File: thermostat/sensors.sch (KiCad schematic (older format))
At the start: 12 parts, among them U2 MCP7940N-xMS, U3 MCP9844, U4 AT24C512, Y3 32.768KHz 20PPM 3.2x1.5mm 7PF

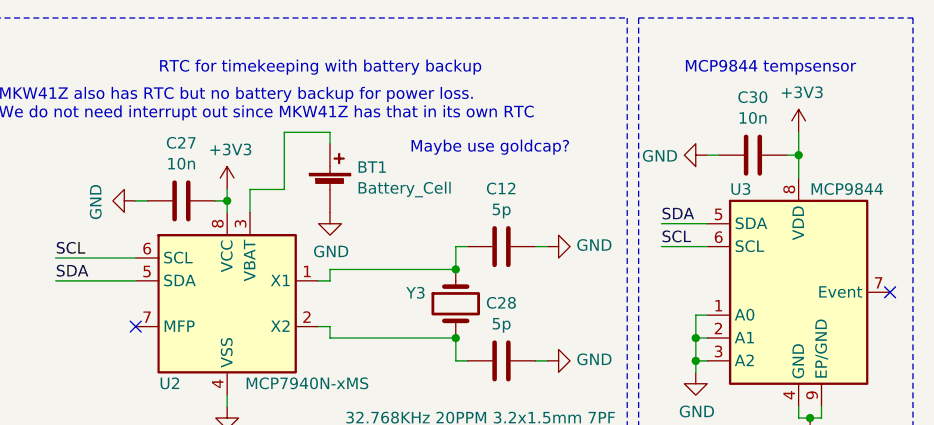
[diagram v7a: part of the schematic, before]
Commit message: Finished layouting tempsensor and thermostat. Parts are ordered from Mouser, PCB ordered from beta-layout.
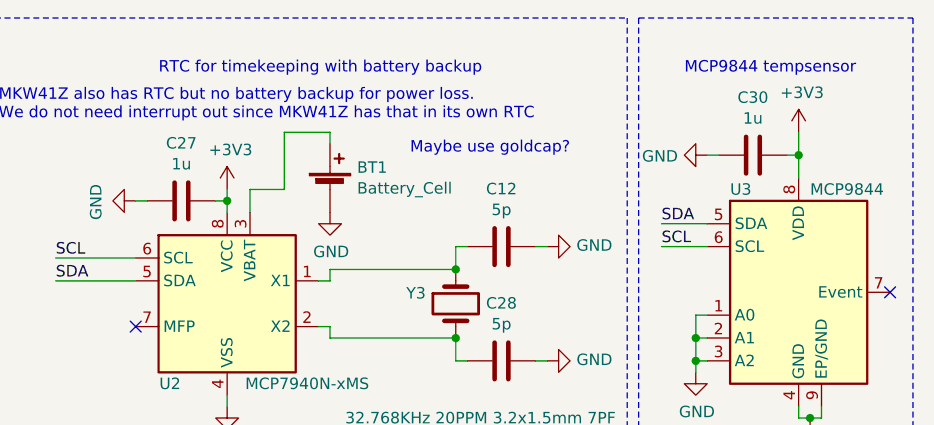
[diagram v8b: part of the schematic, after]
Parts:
- C27, C30: value 10n -> 1u
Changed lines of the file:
@@
 AR Path="/5F32546C/5F32A0D7" Ref="C30"  Part="1"
 F 0 "C30" V 6498 2950 50  0000 C CNN
-F 1 "10n" V 6589 2950 50  0000 C CNN
+F 1 "1u" V 6589 2950 50  0000 C CNN
 F 2 "Capacitor_SMD:C_0603_1608Metric" H 6788 2800 50  0001 C CNN
 F 3 "~" H 6750 2950 50  0001 C CNN
@@
 AR Path="/5F32546C/5F32A0F3" Ref="C27"  Part="1"
 F 0 "C27" V 3998 3150 50  0000 C CNN
-F 1 "10n" V 4089 3150 50  0000 C CNN
+F 1 "1u" V 4089 3150 50  0000 C CNN
 F 2 "Capacitor_SMD:C_0603_1608Metric" H 4288 3000 50  0001 C CNN
 F 3 "~" H 4250 3150 50  0001 C CNN
